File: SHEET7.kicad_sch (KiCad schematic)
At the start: 18 parts, among them U69 RAM_64K_X_1, U70 RAM_64K_X_1, U71 RAM_64K_X_1, U72 RAM_64K_X_1, U73 RAM_64K_X_1, U74 RAM_64K_X_1, U75 RAM_64K_X_1, U76 RAM_64K_X_1, U77 RAM_64K_X_1, U85 RAM_64K_X_1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

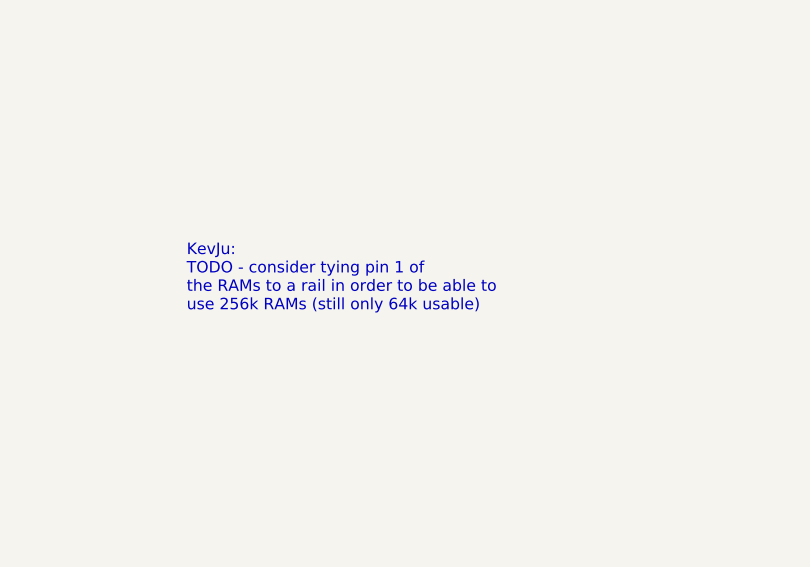
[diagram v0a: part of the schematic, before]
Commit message: added BOM
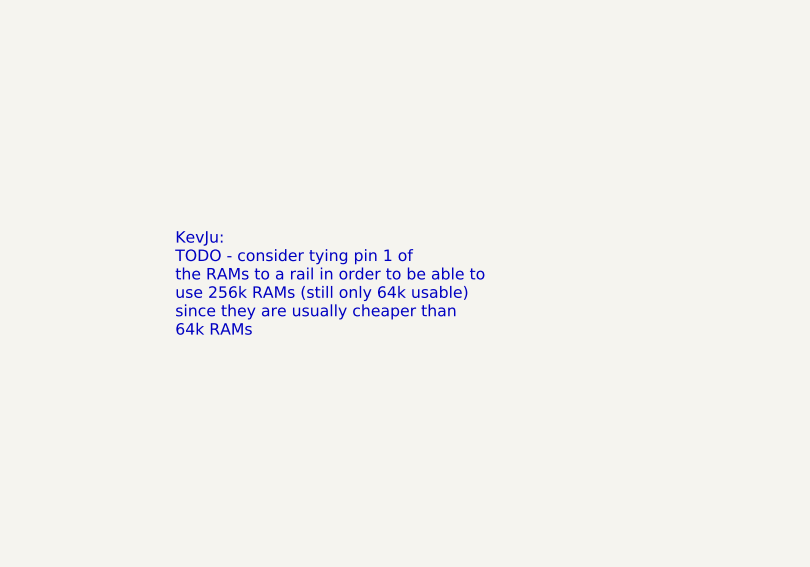
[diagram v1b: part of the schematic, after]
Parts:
- U69, U70, U71, U72, U73, U74, U75, U76, U77, U85, U86, U87, U88, U89, U90, U91, U92, U93: Link (none) -> https://www.jameco.com/z/KM4164B-12-Samsung-Electronics-IC-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
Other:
- note added: "KevJu: TODO - consider tying pin 1 of the RAMs to a rail in order to be able to use 256k RAMs (still only 64k usable) since they are usually cheaper than 64k RAMs"
- note removed: "KevJu: TODO - consider tying pin 1 of the RAMs to a rail in order to be able to use 256k RAMs (still only 64k usable)"
